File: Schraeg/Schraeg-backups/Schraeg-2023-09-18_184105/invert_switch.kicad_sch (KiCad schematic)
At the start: 4 parts

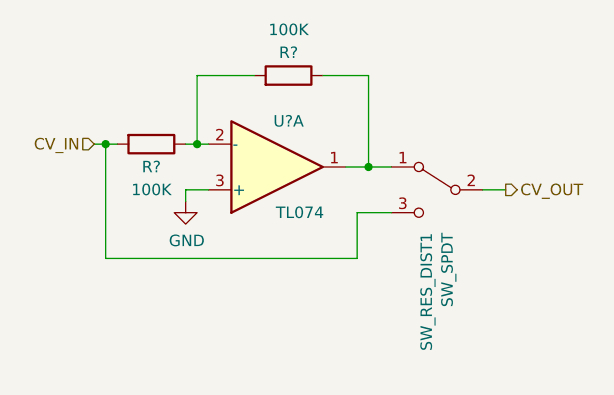
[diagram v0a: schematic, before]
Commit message: fixes filter schematic
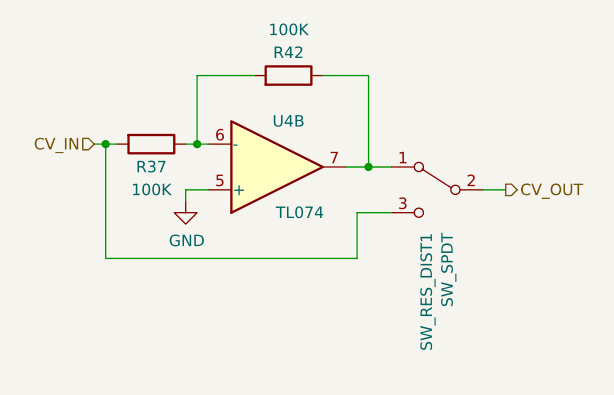
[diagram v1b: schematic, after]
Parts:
- gave numbers to parts that had none: 3
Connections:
- net GND: now also U4.5 (+); no longer U4.3 (+)
- net at R37.1, R42.2: now also U4.6 (-); no longer U4.2 (-)
- net at R42.1, SW_RES_DIST1.1 (A): now also U4.7; no longer U4.1
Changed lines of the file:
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@@
   (symbol (lib_id "power:GND") (at 107.95 97.79 0) (unit 1)
     (in_bom yes) (on_board yes) (dnp no)
-    (property "Reference" "#PWR?" (at 107.95 104.14 0)
+    (property "Reference" "#PWR026" (at 107.95 104.14 0)
       (effects (font (size 1.27 1.27)) hide)
     )
@@
   (symbol (lib_id "Device:R") (at 104.14 91.44 270) (unit 1)
     (in_bom yes) (on_board yes) (dnp no)
-    (property "Reference" "R?" (at 104.14 93.98 90)
+    (property "Reference" "R37" (at 104.14 93.98 90)
       (effects (font (size 1.27 1.27)))
     )
@@
     )
   )
-  (symbol (lib_id "Amplifier_Operational:TL074") (at 118.11 93.98 0) (mirror x) (unit 1)
+  (symbol (lib_id "Amplifier_Operational:TL074") (at 118.11 93.98 0) (mirror x) (unit 2)
     (in_bom yes) (on_board yes) (dnp no)
-    (property "Reference" "U?" (at 119.38 88.9 0)
+    (property "Reference" "U4" (at 119.38 88.9 0)
       (effects (font (size 1.27 1.27)))
     )
@@
   (symbol (lib_id "Device:R") (at 119.38 83.82 270) (mirror x) (unit 1)
     (in_bom yes) (on_board yes) (dnp no)
-    (property "Reference" "R?" (at 119.38 81.28 90)
+    (property "Reference" "R42" (at 119.38 81.28 90)
       (effects (font (size 1.27 1.27)))
     )
